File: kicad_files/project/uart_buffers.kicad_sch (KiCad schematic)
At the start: 5 parts, among them J2 Conn_01x02_Socket, U10 SN74LVC1G125DCKR, U9 SN74LVC1G125DCKR

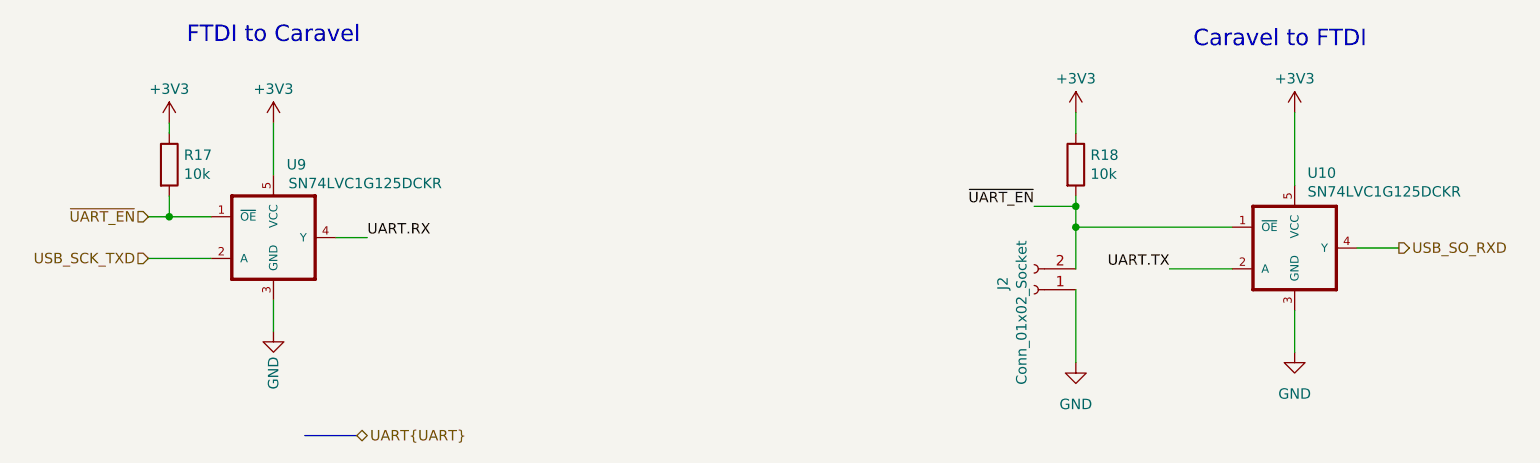
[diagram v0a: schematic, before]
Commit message: started with board layout, also added more stuff on the schematic
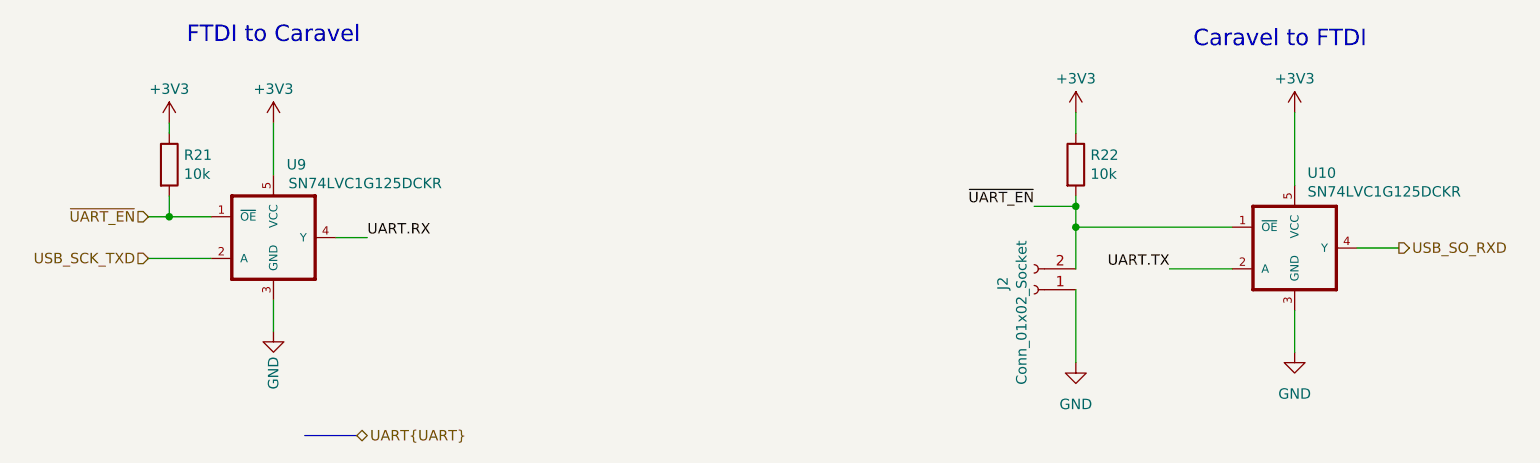
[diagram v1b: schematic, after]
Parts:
- U10, U9: footprint SOT65P210X110-5N -> strive_foot_prints:SOT65P210X110-5N
- renumbered R17 to R21, R18 to R22
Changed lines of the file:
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@@
 		(on_board yes)
 		(dnp no)
-		(property "Reference" "#PWR054"
+		(property "Reference" "#PWR059"
 			(at 92.71 113.03 0)
 			(effects
@@
 			(project "FABulous_board"
 				(path "/5664f05e-a3ef-4177-8026-c4580fa32c71/4820c043-623b-447e-8e47-990cd78f4dc2"
-					(reference "#PWR054")
+					(reference "#PWR059")
 					(unit 1)
 				)
@@
 		(dnp no)
 		(fields_autoplaced yes)
-		(property "Reference" "#PWR055"
+		(property "Reference" "#PWR060"
 			(at 190.5 83.82 0)
 			(effects
@@
 			(project "FABulous_board"
 				(path "/5664f05e-a3ef-4177-8026-c4580fa32c71/4820c043-623b-447e-8e47-990cd78f4dc2"
-					(reference "#PWR055")
+					(reference "#PWR060")
 					(unit 1)
 				)
@@
 		(on_board yes)
 		(dnp no)
-		(property "Reference" "R17"
+		(property "Reference" "R21"
 			(at 81.788 85.1916 0)
 			(effects
@@
 			(project "FABulous_board"
 				(path "/5664f05e-a3ef-4177-8026-c4580fa32c71/4820c043-623b-447e-8e47-990cd78f4dc2"
-					(reference "R17")
+					(reference "R21")
 					(unit 1)
 				)
@@
 		(dnp no)
 		(fields_autoplaced yes)
-		(property "Reference" "#PWR011"
+		(property "Reference" "#PWR057"
 			(at 80.01 85.09 0)
 			(effects
@@
 			(project "FABulous_board"
 				(path "/5664f05e-a3ef-4177-8026-c4580fa32c71/4820c043-623b-447e-8e47-990cd78f4dc2"
-					(reference "#PWR011")
+					(reference "#PWR057")
 					(unit 1)
 				)
@@
 		(dnp no)
 		(fields_autoplaced yes)
-		(property "Reference" "#PWR053"
+		(property "Reference" "#PWR058"
 			(at 92.71 85.09 0)
 			(effects
@@
 			(project "FABulous_board"
 				(path "/5664f05e-a3ef-4177-8026-c4580fa32c71/4820c043-623b-447e-8e47-990cd78f4dc2"
-					(reference "#PWR053")
+					(reference "#PWR058")
 					(unit 1)
 				)
@@
 		(on_board yes)
 		(dnp no)
-		(property "Reference" "#PWR058"
+		(property "Reference" "#PWR063"
 			(at 217.17 115.57 0)
 			(effects
@@
 			(project "FABulous_board"
 				(path "/5664f05e-a3ef-4177-8026-c4580fa32c71/4820c043-623b-447e-8e47-990cd78f4dc2"
-					(reference "#PWR058")
+					(reference "#PWR063")
 					(unit 1)
 				)
@@
 		(on_board yes)
 		(dnp no)
-		(property "Reference" "R18"
+		(property "Reference" "R22"
 			(at 192.278 85.1916 0)
 			(effects
@@
 			(project "FABulous_board"
 				(path "/5664f05e-a3ef-4177-8026-c4580fa32c71/4820c043-623b-447e-8e47-990cd78f4dc2"
-					(reference "R18")
+					(reference "R22")
 					(unit 1)
 				)
@@
 		(on_board yes)
 		(dnp no)
-		(property "Reference" "#PWR056"
+		(property "Reference" "#PWR061"
 			(at 190.5 116.84 0)
 			(effects
@@
 			(project "FABulous_board"
 				(path "/5664f05e-a3ef-4177-8026-c4580fa32c71/4820c043-623b-447e-8e47-990cd78f4dc2"
-					(reference "#PWR056")
+					(reference "#PWR061")
 					(unit 1)
 				)
@@
 			)
 		)
-		(property "Footprint" "SOT65P210X110-5N"
+		(property "Footprint" "strive_foot_prints:SOT65P210X110-5N"
 			(at 217.17 96.52 0)
 			(effects
@@
 			)
 		)
-		(property "Footprint" "SOT65P210X110-5N"
+		(property "Footprint" "strive_foot_prints:SOT65P210X110-5N"
 			(at 92.71 95.25 0)
 			(effects
@@
 		(dnp no)
 		(fields_autoplaced yes)
-		(property "Reference" "#PWR057"
+		(property "Reference" "#PWR062"
 			(at 217.17 83.82 0)
 			(effects
@@
 			(project "FABulous_board"
 				(path "/5664f05e-a3ef-4177-8026-c4580fa32c71/4820c043-623b-447e-8e47-990cd78f4dc2"
-					(reference "#PWR057")
-					(unit 1)
-				)
+					(reference "#PWR062")
+					(unit 1)
+				)

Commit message: misc: simplifiy power pins and other components, add test pins
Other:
- title: (none) -> UART Buffers
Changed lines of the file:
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@@
 	(paper "A4")
 	(title_block
+		(title "UART Buffers")
 		(date "2024-05-30")
 		(rev "0.1")
